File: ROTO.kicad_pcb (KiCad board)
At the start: 2 copper layers, 7 parts, among them J1 POWER INPUT, J2 RELAY, J3 SWITCH, U1 LM7805, U2 SX1509

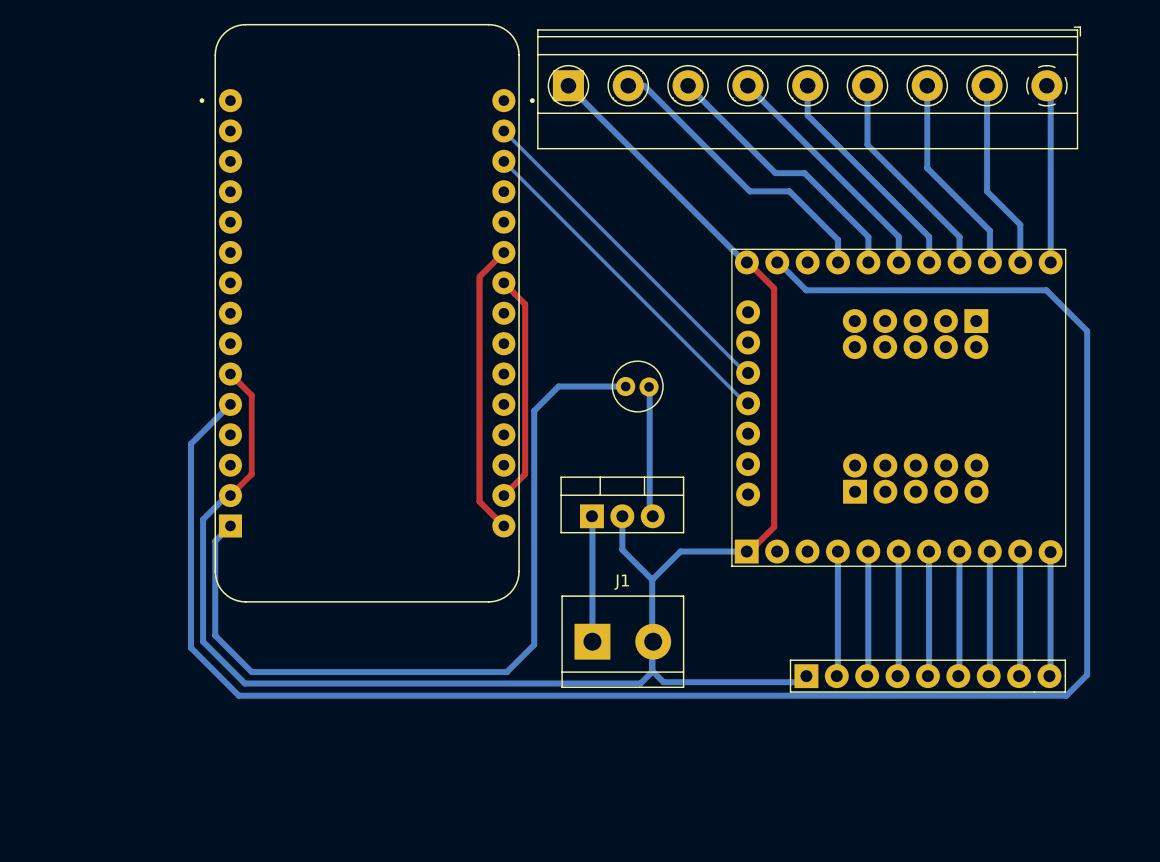
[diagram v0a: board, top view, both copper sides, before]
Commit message: Flipped PCB
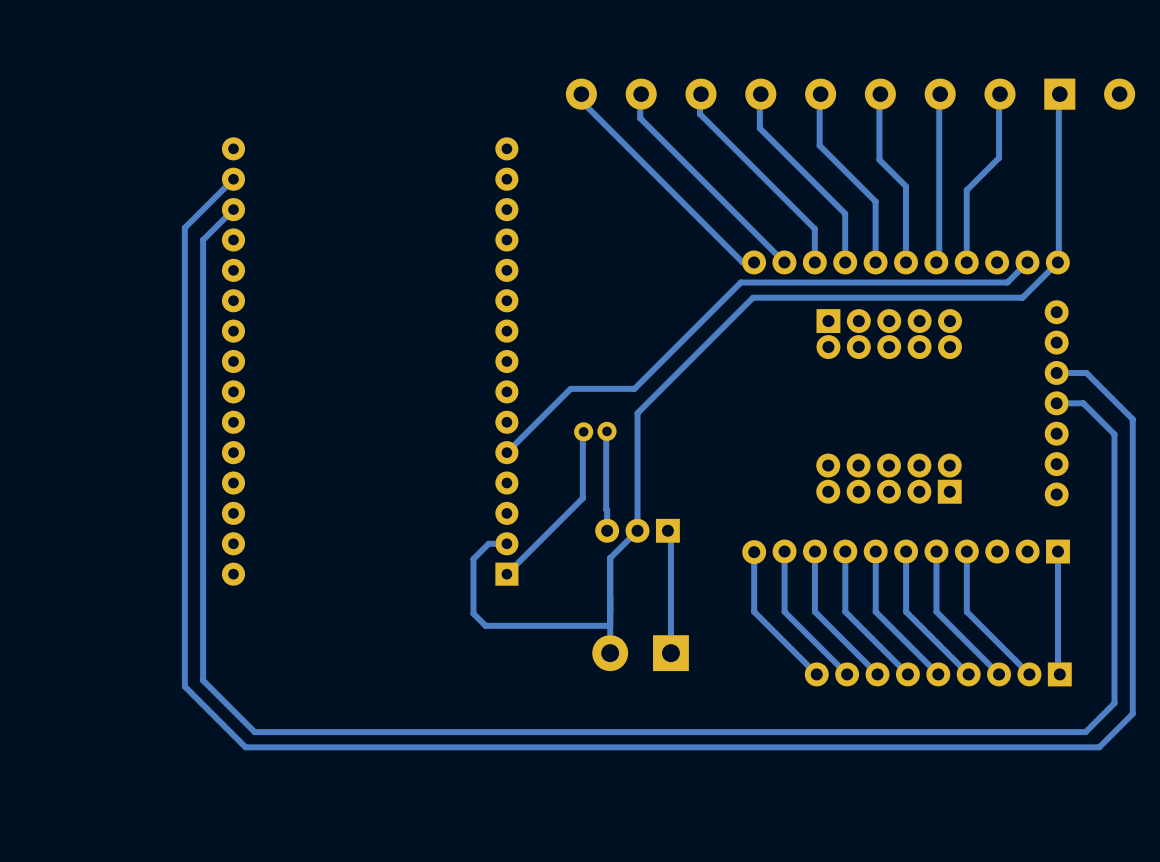
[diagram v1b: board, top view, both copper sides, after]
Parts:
- A1, C1, J1, J2, U1, U2: moved to B.Cu
- J3: value SWITCH -> Switch; footprint TerminalBlock_Phoenix:TerminalBlock_Phoenix_MKDS-1,5-9_1x09_P5.00mm_Horizontal -> TerminalBlock_Phoenix:TerminalBlock_Phoenix_MKDS-1,5-10_1x10_P5.00mm_Horizontal; moved to B.Cu
- moved J2 19.5 mm to (165.1, 116.3)
- moved J1 6.63 mm to (152.9, 114.6), turned to 180 degrees
- moved U1 6.46 mm to (152.7, 104.3), turned to 180 degrees
- moved J3 6.12 mm to (190.4, 67.8)
- moved C1 4.28 mm to (147.3, 96.0), turned to 180 degrees
- moved A1 4.04 mm to (127.8, 90.2), turned to 180 degrees
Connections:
- C1 pad 1: +5V -> Net-(U1-VO)
- C1 pad 2: Net-(U1-VO) -> +5V
- J3 pad 1: Net-(J3-Pin_1) -> unconnected-(J3-Pin_1-Pad1)
- J3 pad 2: Net-(J3-Pin_2) -> GND
- J3 pad 9: GND -> Net-(J3-Pin_9)
- U2 pad 12: Net-(J3-Pin_1) -> Net-(J3-Pin_10)
- U2 pad 13: Net-(J3-Pin_2) -> Net-(J3-Pin_9)
- U2 pad 14: Net-(J3-Pin_3) -> Net-(J3-Pin_8)
- U2 pad 15: Net-(J3-Pin_4) -> Net-(J3-Pin_7)
- U2 pad 16: Net-(J3-Pin_5) -> Net-(J3-Pin_6)
- U2 pad 17: Net-(J3-Pin_6) -> Net-(J3-Pin_5)
- U2 pad 18: Net-(J3-Pin_7) -> Net-(J3-Pin_4)
- U2 pad 19: Net-(J3-Pin_8) -> Net-(J3-Pin_3)
- U2 pad 25: GND -> unconnected-(U2C-GND-Pad25)
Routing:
- net Net-(A1B-D1): track 29.4 -> 159.2 mm
- net Net-(A1B-D2): track 29.2 -> 147.8 mm
- net +3.3V: track 156.1 -> 50.1 mm
- net +5V: track 67.1 -> 14.6 mm
- net GND: track 151.5 -> 112.2 mm
- net unconnected-(A1B-3V3-PadJ2_15): track 25.2 -> 0.00 mm
- net Net-(J3-Pin_10): track 0.00 -> 20.1 mm
- net unconnected-(A1B-GND-PadJ2_14): track 19.3 -> 0.00 mm
- net Net-(J3-Pin_9): track 0.00 -> 18.6 mm
- net Net-(J3-Pin_2): track 15.9 -> 0.00 mm
- net Net-(J3-Pin_1): track 14.9 -> 0.00 mm
- net Net-(J3-Pin_8): track 24.8 -> 17.5 mm
- net Net-(J3-Pin_7): track 22.9 -> 16.5 mm
- net Net-(J3-Pin_5): track 19.0 -> 14.5 mm
- net Net-(J3-Pin_6): track 20.0 -> 15.5 mm
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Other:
- board text added: "Designed By - Yug Thapar (Solvrz Inc.)"
- board text removed: "Designed By - SOLVRZ INC."

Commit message: Updated PDF
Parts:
- moved A1 15.1 mm to (114.6, 97.5)
- moved C1 15.1 mm to (134.1, 103.4)
- moved J1 15.1 mm to (139.7, 121.9)
- moved J2 15.1 mm to (151.9, 123.7)
- moved J3 15.1 mm to (177.2, 75.2)
- moved U1 15.1 mm to (139.4, 111.7)
- moved U2 15.1 mm to (159.1, 101.2)
